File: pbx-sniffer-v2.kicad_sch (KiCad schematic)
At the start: 1 part, among them U1 STM32NucleoF303RE

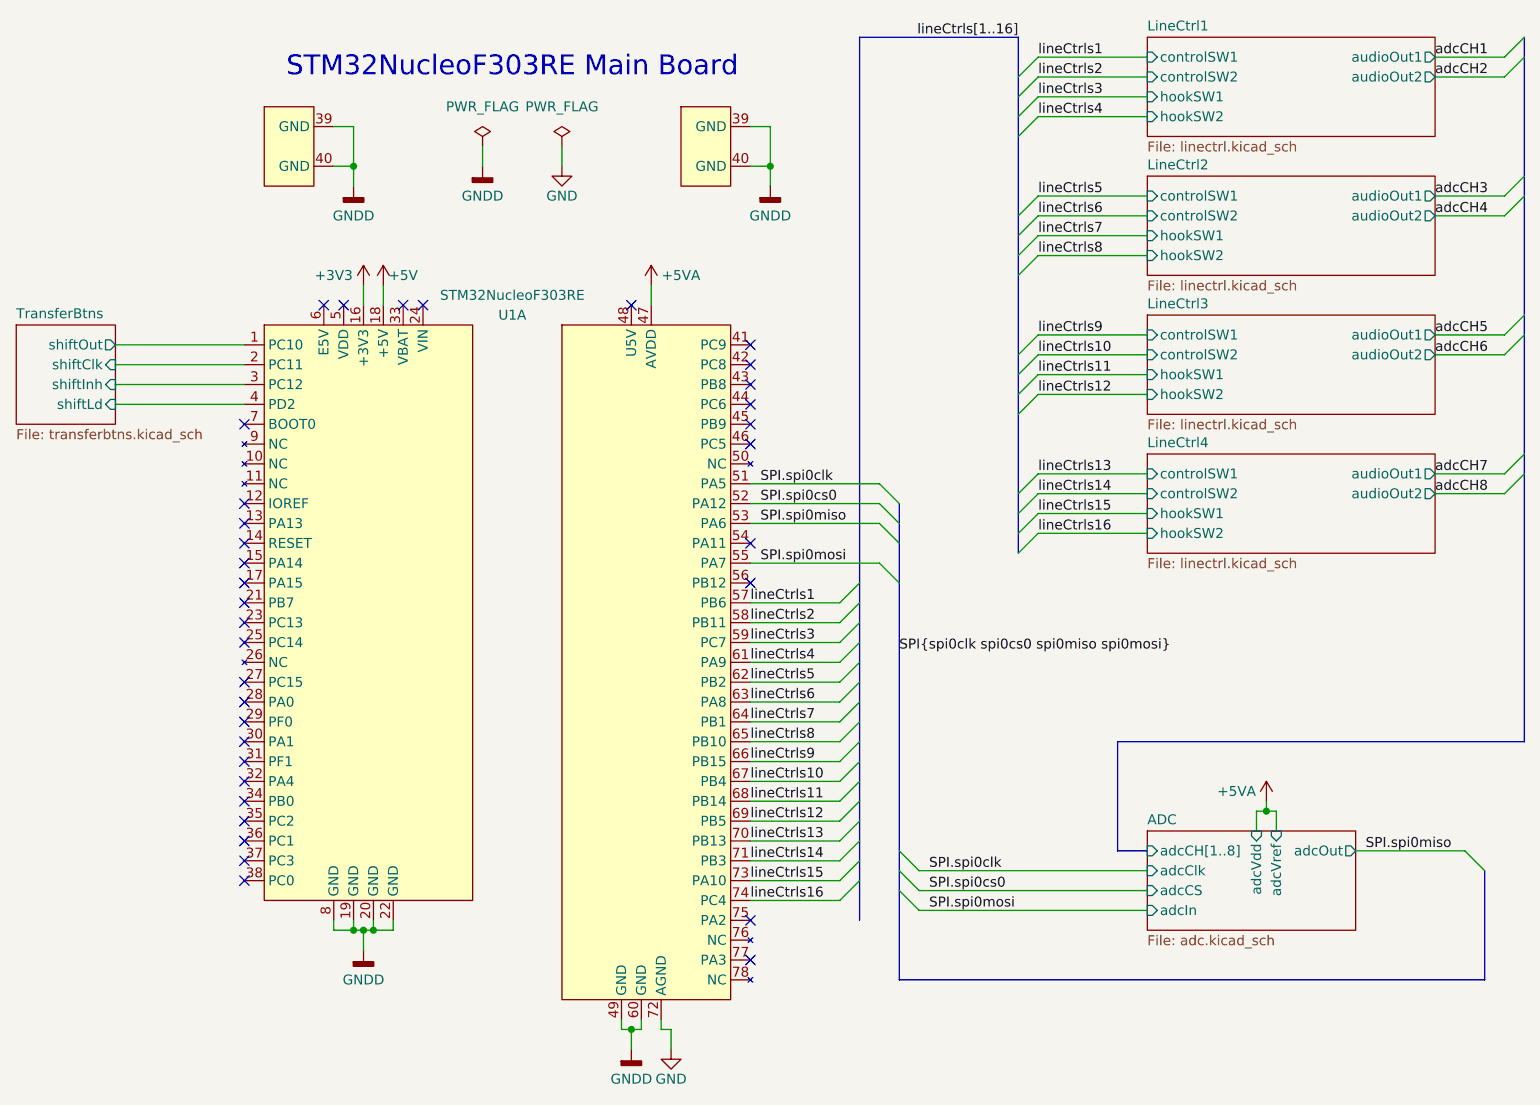
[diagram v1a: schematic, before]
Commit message: add initial supporting power circuitry for stm32f303re
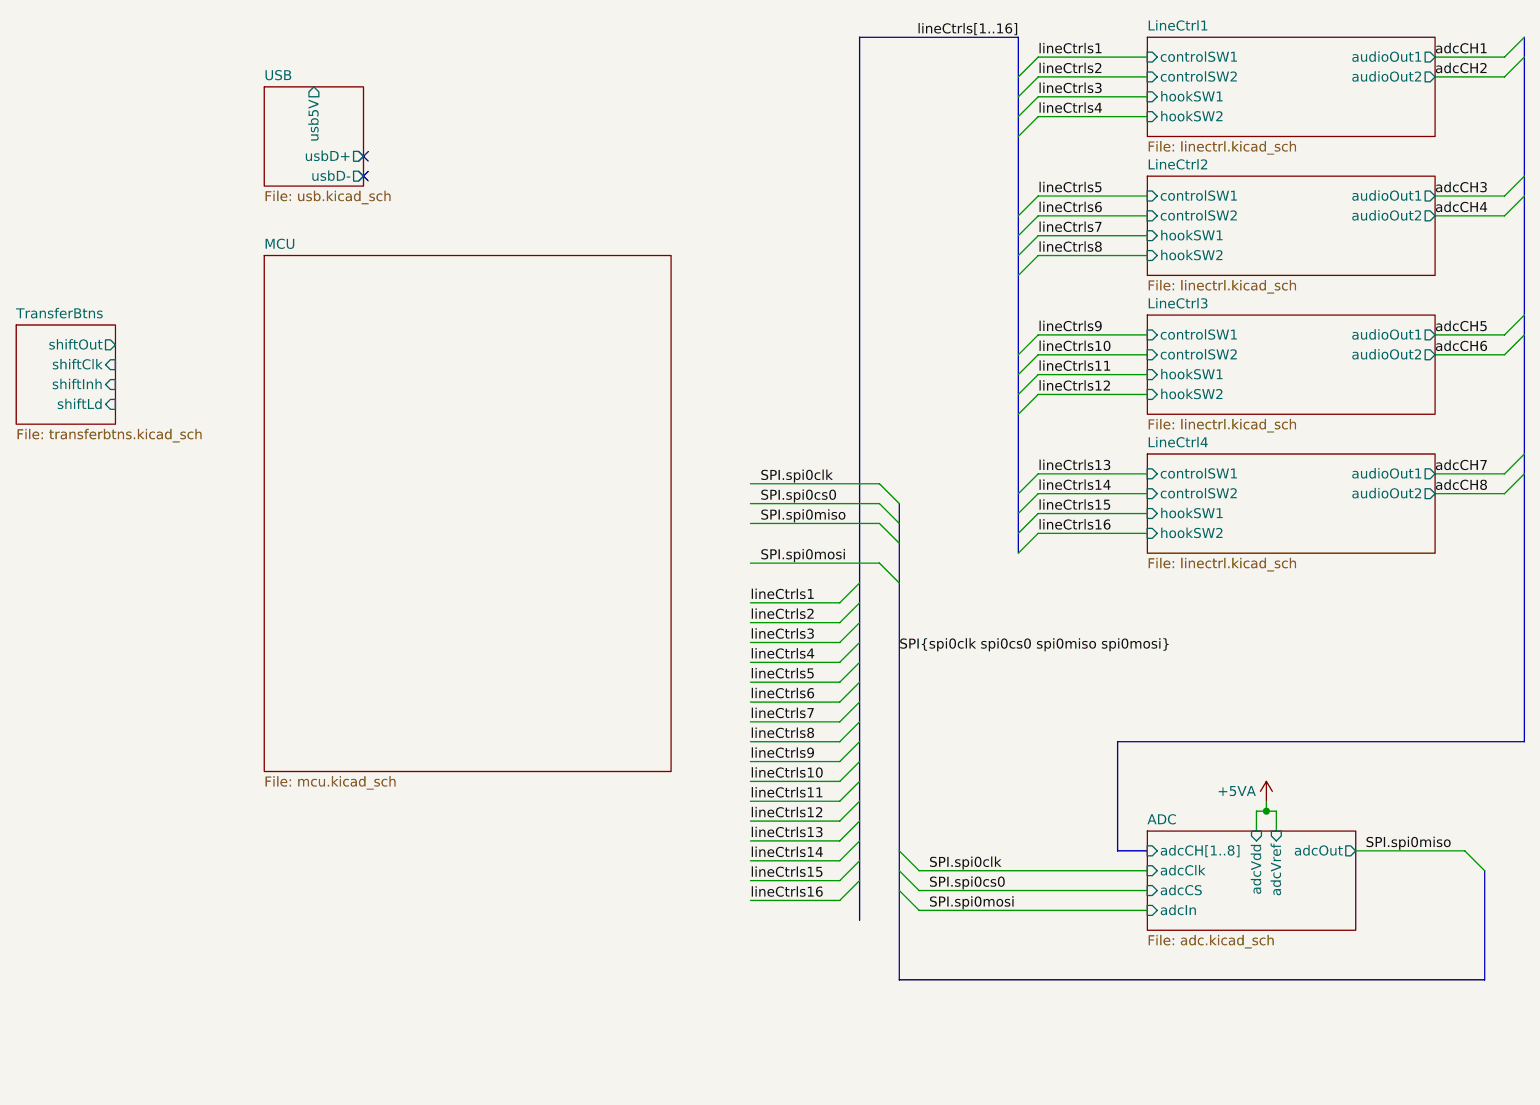
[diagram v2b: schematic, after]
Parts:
- removed U1: STM32NucleoF303RE, Nucleo:STM32NucleoF303RE, symbol Nucleo:STM32NucleoF303RE
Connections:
- no-connect marks 35 -> 2
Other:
- added sheet MCU (mcu.kicad_sch)
- added sheet USB (usb.kicad_sch)
- note removed: "STM32NucleoF303RE Main Board"
